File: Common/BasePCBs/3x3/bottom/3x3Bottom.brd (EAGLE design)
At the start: 100 x 80 mm, 10 parts, among them CON1 SHIELD_FINGER0820, CON2 SHIELD_FINGER0820, CON3 SHIELD_FINGER0820, CON4 SHIELD_FINGER0820, CON5 SHIELD_FINGER0820, CON6 SHIELD_FINGER0820, CON7 SHIELD_FINGER0820, CON8 SHIELD_FINGER0820, CON9 SHIELD_FINGER0820

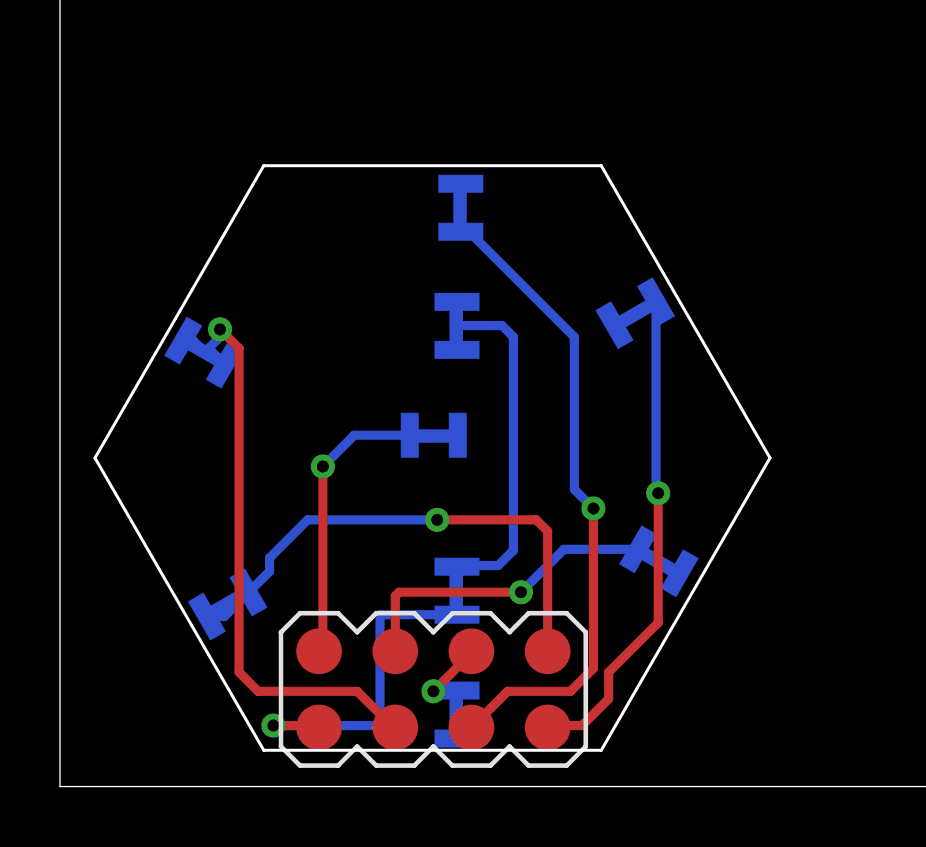
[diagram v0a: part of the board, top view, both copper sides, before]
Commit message: updated the Programmable OLED PCB. now cleaner, need to go a final iteration on it
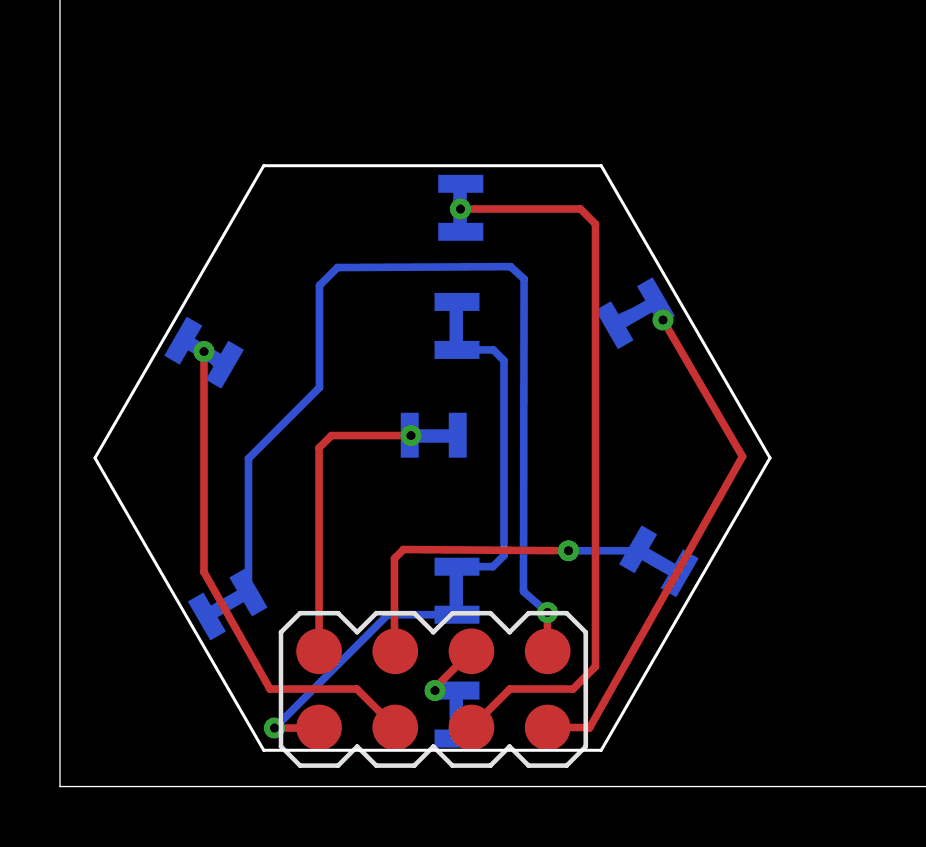
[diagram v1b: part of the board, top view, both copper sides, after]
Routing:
- net SOUT2: track 17.1 -> 32.8 mm
- net SOUT1: track 21.4 -> 28.3 mm
- net VCC: track 26.2 -> 22.3 mm
- net SIN2: track 16.4 -> 19.4 mm
- net SOUT3: track 10.6 -> 13.0 mm
- net SIN1: track 2.66 -> 4.15 mm
- net SIN3: track 20.4 -> 19.0 mm
- net GND: track 11.1 -> 11.7 mm

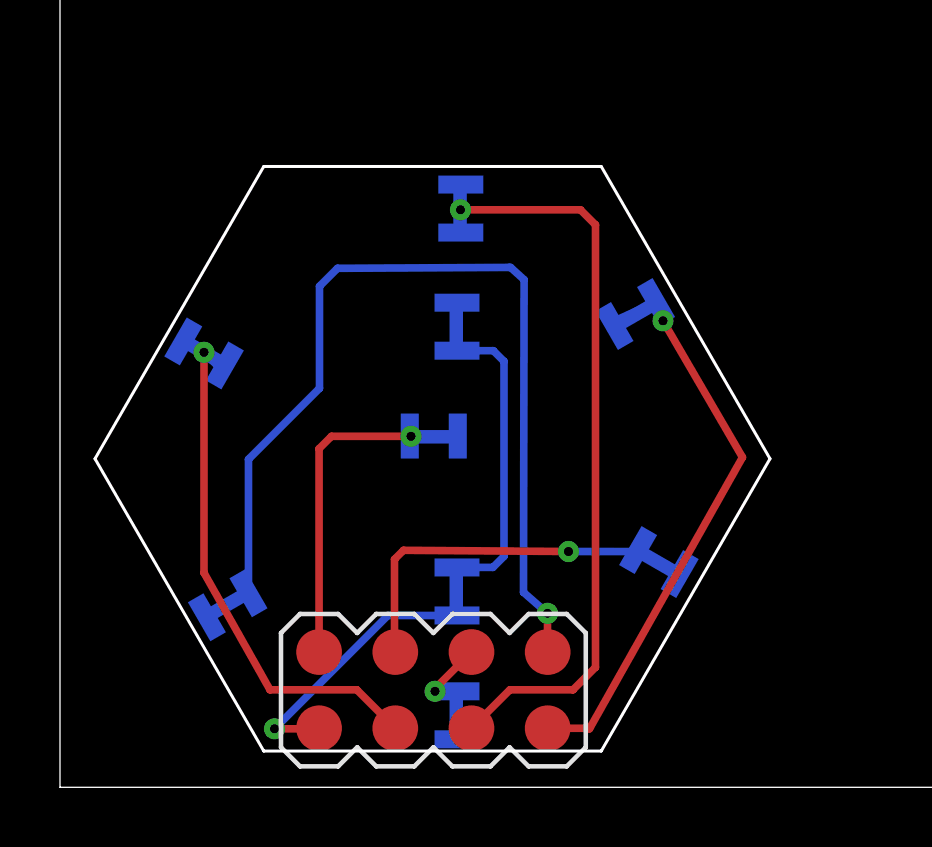
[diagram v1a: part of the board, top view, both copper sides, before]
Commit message: fixed incorrect connections for the 3x3Bottom PCB
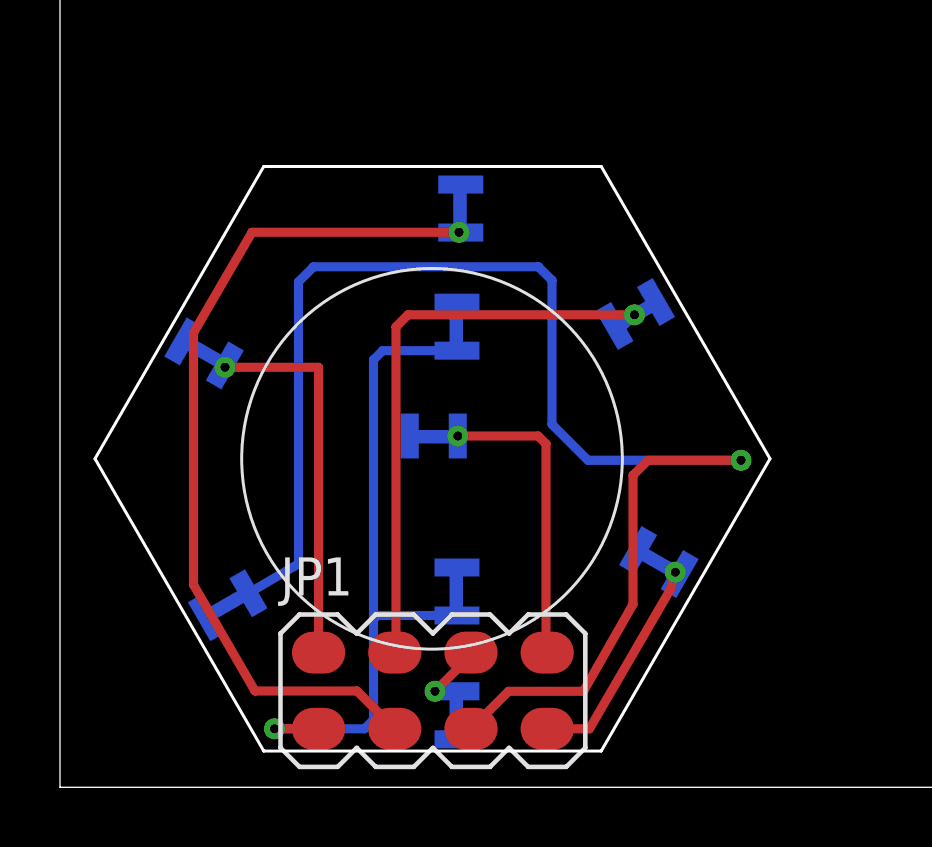
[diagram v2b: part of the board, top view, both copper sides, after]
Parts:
- JP1: device MakerWear:2X4 -> MakerWear:M04X2_0.1"_PADS
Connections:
- net GND: now also JP1.8; no longer JP1.P$8
- net SIN1: now also JP1.6; no longer JP1.P$6
- net SIN2: now also JP1.4; no longer JP1.P$4
- net SIN3: now also JP1.2; no longer JP1.P$2
- net SOUT1: now also JP1.3; no longer JP1.P$3
- net SOUT2: now also JP1.5; no longer JP1.P$5
- net SOUT3: now also JP1.7; no longer JP1.P$7
- net VCC: now also JP1.1; no longer JP1.P$1
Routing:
- net SOUT2: track 32.8 -> 49.2 mm
- net SIN3: track 19.0 -> 14.3 mm
- net VCC: track 22.3 -> 25.8 mm
- net SOUT3: track 13.0 -> 10.4 mm
- net SIN2: track 19.4 -> 21.4 mm
- net SOUT1: track 28.3 -> 30.1 mm
